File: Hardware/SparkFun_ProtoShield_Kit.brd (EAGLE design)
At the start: 53.3 x 68.6 mm, 29 parts

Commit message: Add files via upload
-updated labels and silkscreen
-changed names to vectors
-flipped the BlueSMiRF header's orientation so that the bluetooth faces out away from the board
-modified traces for the BlueSMiRF
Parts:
- JP2: value (none) -> BlueSMiRF
- JP7: value BlueSMiRF -> (none)
- moved U$1 51.0 mm to (9.53, 6.86)
- moved JP2 12.7 mm to (29.2, 66.7), turned to 180 degrees
- moved JP7 12.7 mm to (29.2, 62.4), turned to 180 degrees
- turned JP9 to 270 degrees
- turned SJ3 to 0 degrees
- renumbered S3 to S2
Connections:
- net FTDI_5V renamed VCC
- net FTDI_RX renamed TX-O
- net FTDI_TX renamed RX-I
- net RES renamed BUTTON
- removed net FTDI_GND: JP2.3, JP7.3, SJ3.1
- net GND: now also JP2.3, JP7.3, SJ3.1
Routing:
- net GND: track 24.7 -> 34.0 mm
- net FTDI_GND: track 7.30 -> 0.00 mm
- net VCC: track 11.2 -> 17.6 mm, vias 0 -> 1
- net RX-I: track 13.2 -> 19.5 mm, vias 0 -> 1
- net TX-O: track 14.5 -> 18.6 mm
- net LED1: track 24.3 -> 23.7 mm
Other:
- board text added: "+"
- board text added: "-"
- board text added: "Toni Klopfenstein & Ho Yun "Bobby" Chan"
- board text added: "v31"
- board text removed: "JC1"
- board text removed: "JC2"
- board text removed: "JC3"
- board text removed: "Toni Klopfenstein"
- board text removed: "v30"

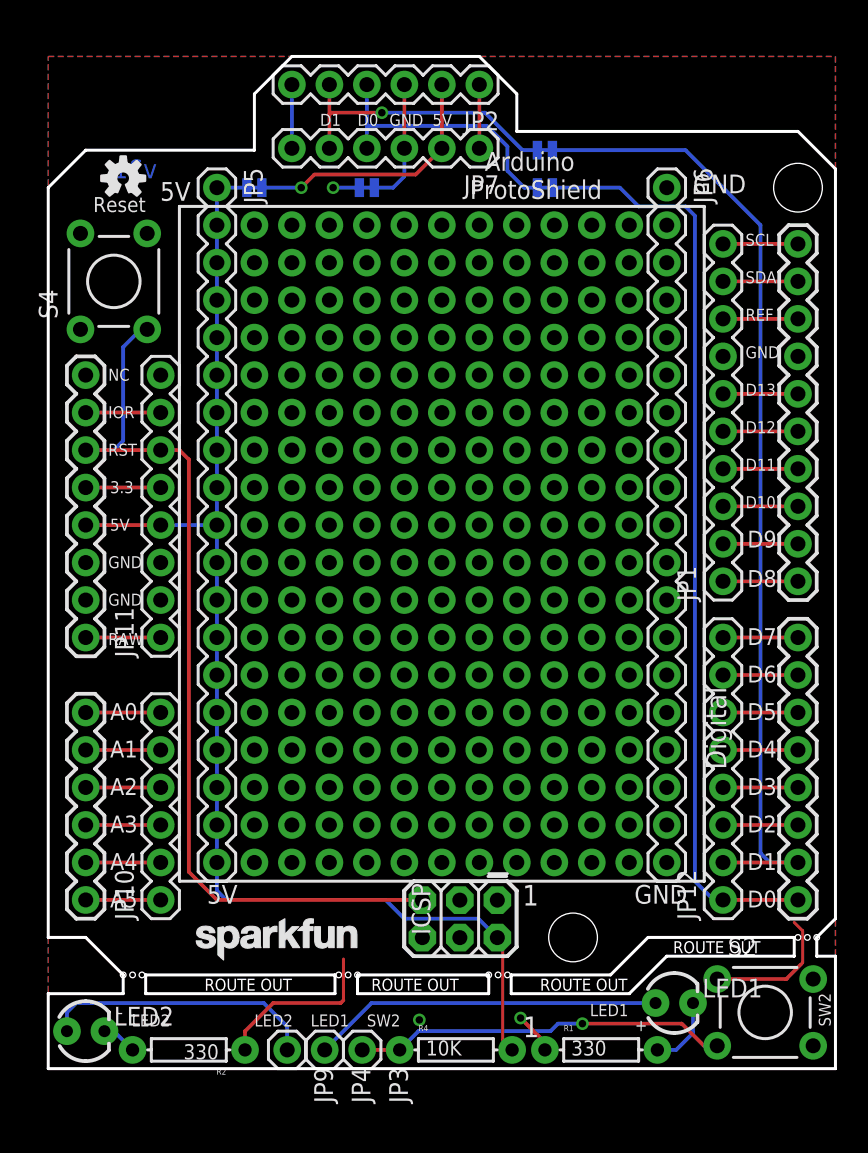
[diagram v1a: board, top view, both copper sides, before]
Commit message: Update files
**Board**

* Align the 5V/GND silk screen.
* Replace the SparkFun logo with a SparkFun logo w/flame, in the SparkFun Aesthetics library.
* Add the silk for the Arduino PTH headers on the bottom side as well. 
* Fix placement and size of the BlueSMiRF text on the underside of the shield. 
* Add silkscreen for the UART pins for BlueSMiRF.
* Add copper boundary around GND trace so that it can be easily cut.
* Adjust position of prototyping hardware header.

**Schematic**

* Change all text to “vector”.
* Change the labels for the various boxes so they are the same ratio and size. 
* Change all dashed lines to “Short Dash”.
* Update all outdated packages to our current Sparkfun Library packages (i.e. GND symbols are not current, 5V arrow, Switches, etc. ).
* Place the Open Hardware symbol next to the SparkFun symbol. 
* Net the GND net flag on the BlueSMiRF header to a GND symbol. 
* Update the wires on the ISCP header to indicate that the MISO and MOSI lines are not connected to anything on the proto (i.e.“MOSI NC” flag).
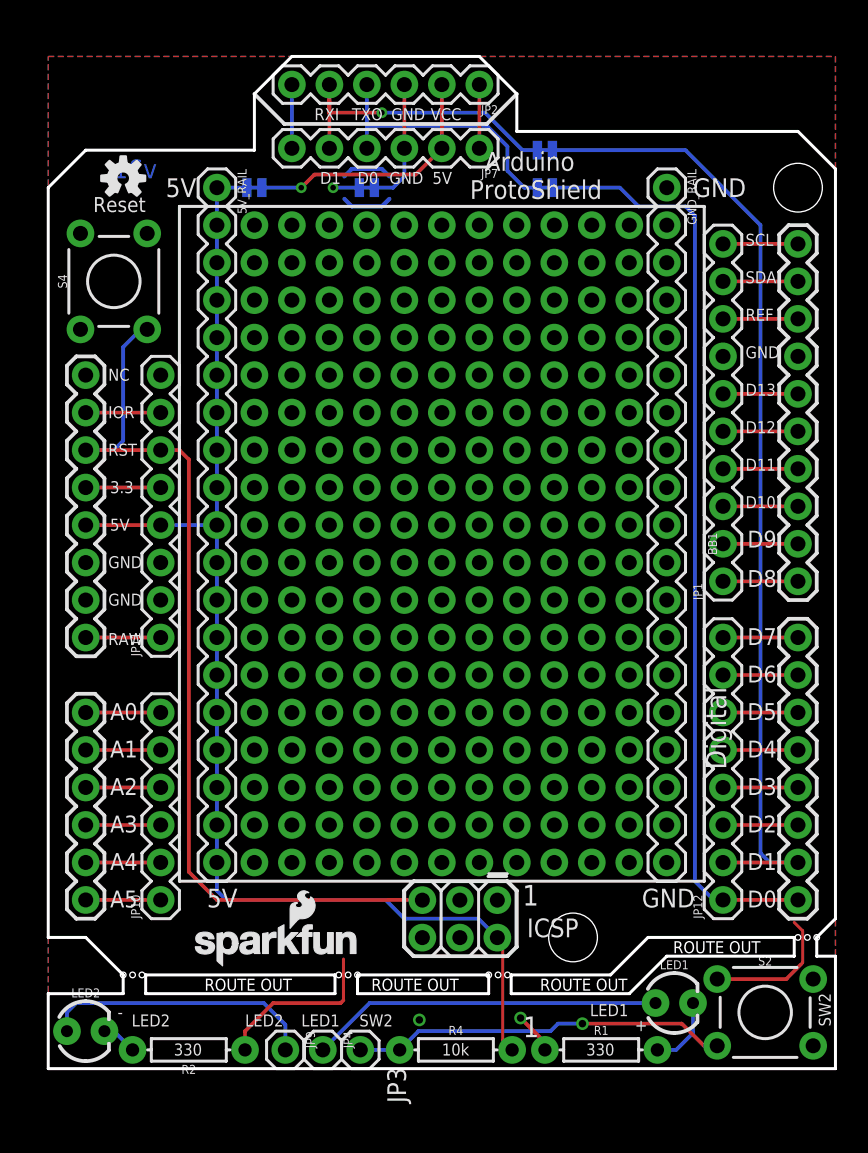
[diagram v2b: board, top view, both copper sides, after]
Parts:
- JP11, JP12: device SparkFun-Connectors:1X08_ROUND -> SparkFun-Connectors:1X08
- LED1, LED2: device SparkFun-LED:LED3MM -> SparkFun-LED:LED_3MM
- R4: value 10K -> 10k
- S2, S4: value SWITCH-MOMENTARY-2PTH -> MOMENTARY-SWITCH-SPST-PTH-6.0MM-KIT; device SparkFun-Electromechanical:TACTILE-PTH -> SparkFun-Switches:TACTILE_SWITCH_PTH_6.0MM_KIT
- SJ1, SJ2, SJ3, SJ4: value JUMPER-PAD-2-NC_BY_TRACE -> JUMPER-SMT_2_NC_TRACE_SILK; device SparkFun-Passives:PAD-JUMPER-2-NC_BY_TRACE_YES_SILK -> SparkFun-Jumpers:SMT-JUMPER_2_NC_TRACE_SILK
- U$1: value SFE_LOGO_NAME.1_INCH -> SFE_LOGO_NAME_FLAME.1_INCH; device SparkFun-Aesthetics:SFE_LOGO_NAME_.1 -> SparkFun-Aesthetics:SFE_LOGO_NAME_FLAME_.1
- moved BB1 29.0 mm to (26.7, 35.6)
- moved JP3 0.13 mm to (21.1, 1.27)
- moved JP4 0.13 mm to (18.6, 1.27)
- moved JP9 0.13 mm to (16.1, 1.27)
- renumbered JP5 to 5V_RAIL, JP6 to GND_RAIL
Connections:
- net MISO renamed MISO_NC
- net MOSI renamed MOSI_NC
- net N$185 renamed VIN
- net N$8 renamed 3.3
- net SCK renamed SCK_NC
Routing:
- net N$2: track 0.00 -> 3.47 mm
- net N$9: track 0.00 -> 3.47 mm
- net RX-I: track 19.5 -> 21.4 mm
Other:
- board text added: "10k"
- board text added: "330"
- board text added: "RXI"
- board text added: "TXO"
- board text added: "VCC"
